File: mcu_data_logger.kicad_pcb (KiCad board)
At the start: 2 copper layers, 29 parts, among them J1 Conn_01x04_Pin, J2 Conn_01x09_Pin, J3 Conn_01x04_Pin, J4 Conn_02x03_Odd_Even, U1 24LC1025, U2 DS1337S_, U3 24LC1025, U4 ATMEGA328P-AU, Y1 32.768 kHz, Y2 16MHz

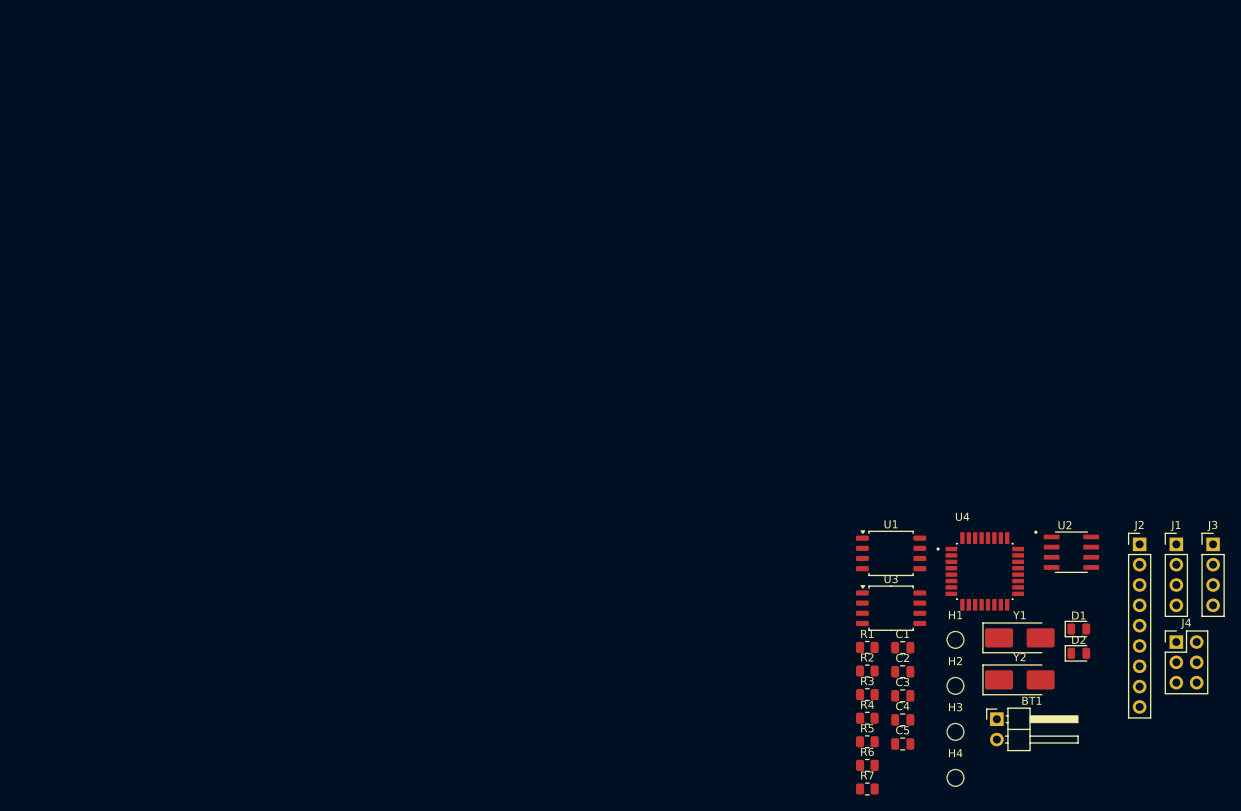
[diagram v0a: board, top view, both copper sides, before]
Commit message: Partial arrangement of footprints and change of battery component footprint
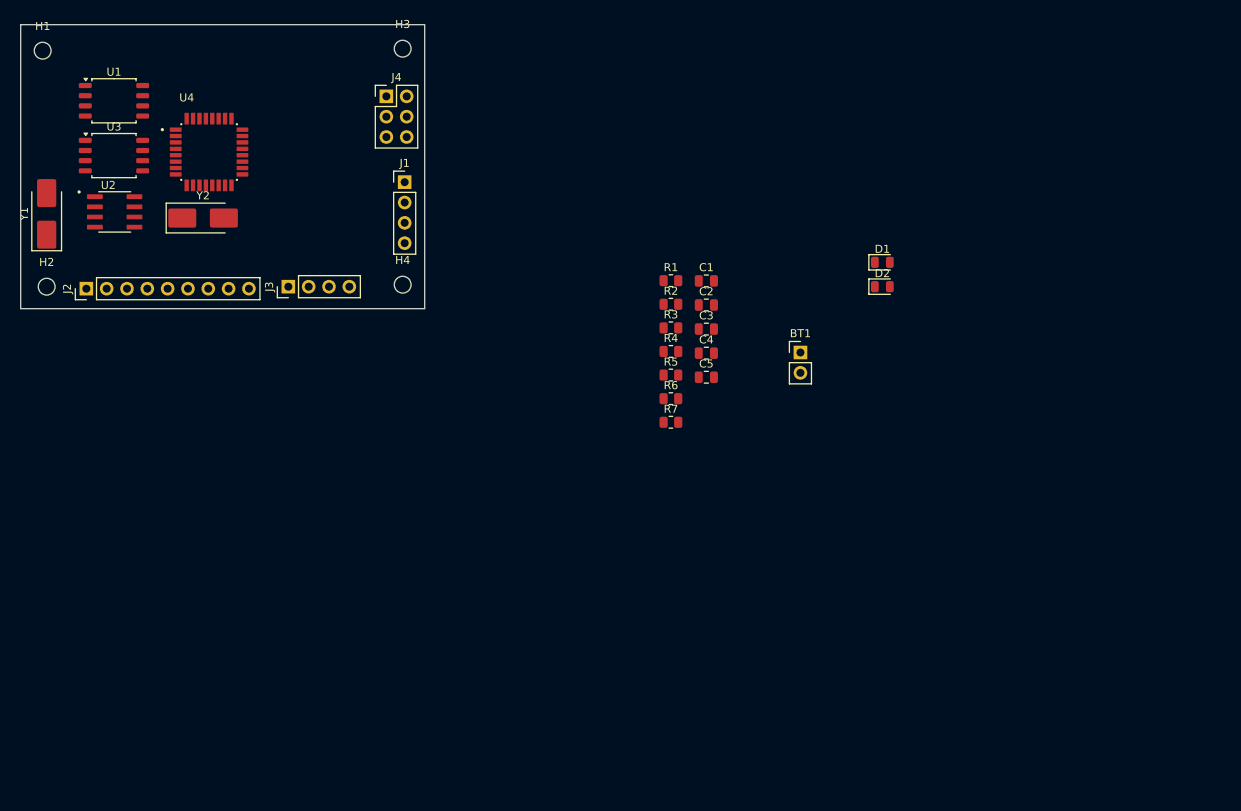
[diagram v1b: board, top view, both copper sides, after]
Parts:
- BT1: footprint Connector_PinHeader_2.54mm:PinHeader_1x02_P2.54mm_Horizontal -> Connector_PinHeader_2.54mm:PinHeader_1x02_P2.54mm_Vertical
- moved H1 135.8 mm to (73.2, 59.8)
- moved J2 135.5 mm to (78.7, 89.5), turned to 90 degrees
- moved Y1 132.7 mm to (73.8, 80.2), turned to 90 degrees
- moved U2 126.9 mm to (82.2, 79.9)
- moved H2 124.1 mm to (73.8, 89.2)
- moved J4 120.0 mm to (116.2, 65.5)
- moved J3 120.0 mm to (104.0, 89.2), turned to 90 degrees
- moved Y2 117.3 mm to (93.3, 80.7)
- moved U1 112.4 mm to (82.2, 66.0)
- moved U3 112.4 mm to (82.2, 72.9)
- moved U4 110.2 mm to (94.0, 72.4)
- moved H3 109.9 mm to (118.2, 59.5)
- moved J1 106.6 mm to (118.5, 76.2)
- moved H4 92.6 mm to (118.2, 89.0)
- moved R1 52.0 mm to (151.8, 88.5)
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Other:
- board outline added: 50.5 x 35.5 mm

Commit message: footprint arrangement and placement complete
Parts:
- moved BT1 97.5 mm to (75.2, 67.2)
- moved D2 76.6 mm to (105.5, 62.0), turned to 180 degrees
- moved D1 73.9 mm to (109.5, 62.0)
- moved R1 71.1 mm to (81.0, 82.0)
- moved C1 70.0 mm to (91.5, 61.8)
- moved C3 68.8 mm to (95.7, 61.8)
- moved C5 68.3 mm to (100.0, 61.8)
- moved R2 67.2 mm to (85.2, 82.0), turned to 180 degrees
- moved R7 61.0 mm to (105.5, 66.5)
- moved R5 54.1 mm to (109.5, 66.5)
- moved R4 53.4 mm to (105.5, 70.8), turned to 180 degrees
- moved C4 53.3 mm to (105.5, 81.0), turned to 180 degrees
- moved R6 53.1 mm to (109.8, 70.8)
- moved C2 52.6 mm to (105.5, 77.5)
- moved R3 50.5 mm to (105.5, 74.2)
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- renumbered D2 to D1, D1 to D2
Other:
- board size 50.5 x 35.5 mm -> 48 x 34.5 mm

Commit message: initial routing done
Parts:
- moved U1 6.87 mm to (82.7, 69.6)
- moved U3 6.85 mm to (83.2, 62.8)
- moved H4 1.82 mm to (117.0, 90.0)
- moved H2 1.75 mm to (73.7, 90.0)
- moved H3 0.48 mm to (117.0, 59.8)
- moved H1 0.23 mm to (73.7, 59.8)
- moved J2 0.22 mm to (78.5, 88.5)
- moved J3 0.22 mm to (103.7, 88.2)
- moved C1 0.18 mm to (91.5, 62.0)
- moved C3 0.18 mm to (95.8, 62.0)
- moved C5 0.18 mm to (100.0, 62.0)
- turned C2 to 180 degrees
- turned D2 to 0 degrees
- turned R3 to 180 degrees
- turned R5 to 180 degrees
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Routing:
- net /Vcc: track 0.00 -> 114.3 mm, vias 0 -> 1
- net /SCK: track 0.00 -> 95.5 mm, vias 0 -> 3
- net Net-(BT1-+): track 0.00 -> 56.7 mm, vias 0 -> 3
- net /SDA: track 0.00 -> 55.7 mm, vias 0 -> 2
- net GND: track 0.00 -> 50.4 mm, vias 0 -> 6
- net /TX: track 0.00 -> 30.0 mm, vias 0 -> 1
- net /RX: track 0.00 -> 28.7 mm, vias 0 -> 1
- net /D2: track 0.00 -> 26.6 mm, vias 0 -> 1
- net /MOSI: track 0.00 -> 26.1 mm
- net /RESET: track 0.00 -> 26.0 mm, vias 0 -> 2
- net Net-(U4-PB7): track 0.00 -> 25.6 mm, vias 0 -> 2
- net /D3: track 0.00 -> 25.2 mm
- net Net-(U4-PB6): track 0.00 -> 23.8 mm
- net /D4: track 0.00 -> 22.2 mm
- net /MISO: track 0.00 -> 21.2 mm, vias 0 -> 1
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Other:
- board size 48 x 34.5 mm -> 48 x 36 mm

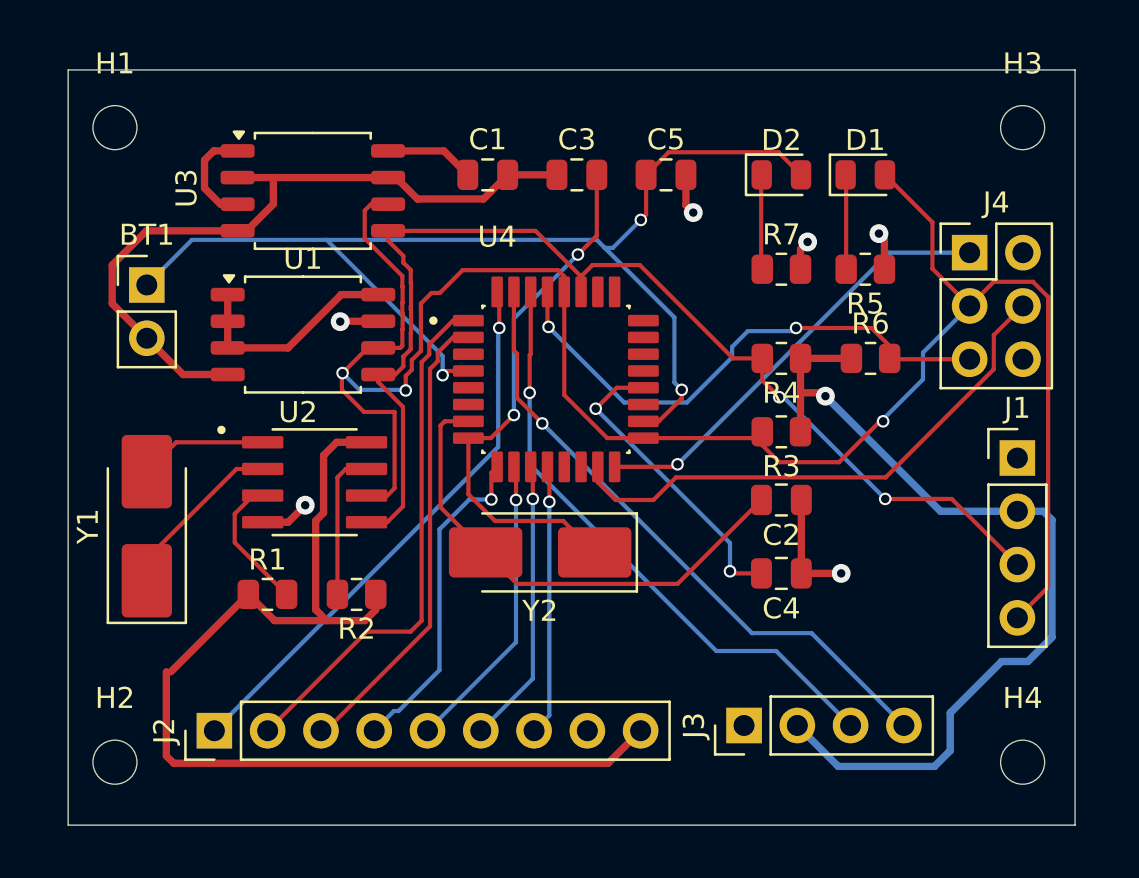
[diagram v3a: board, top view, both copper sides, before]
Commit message: added copper fills for the /Vcc and GND nets, front and back copper layer respectively
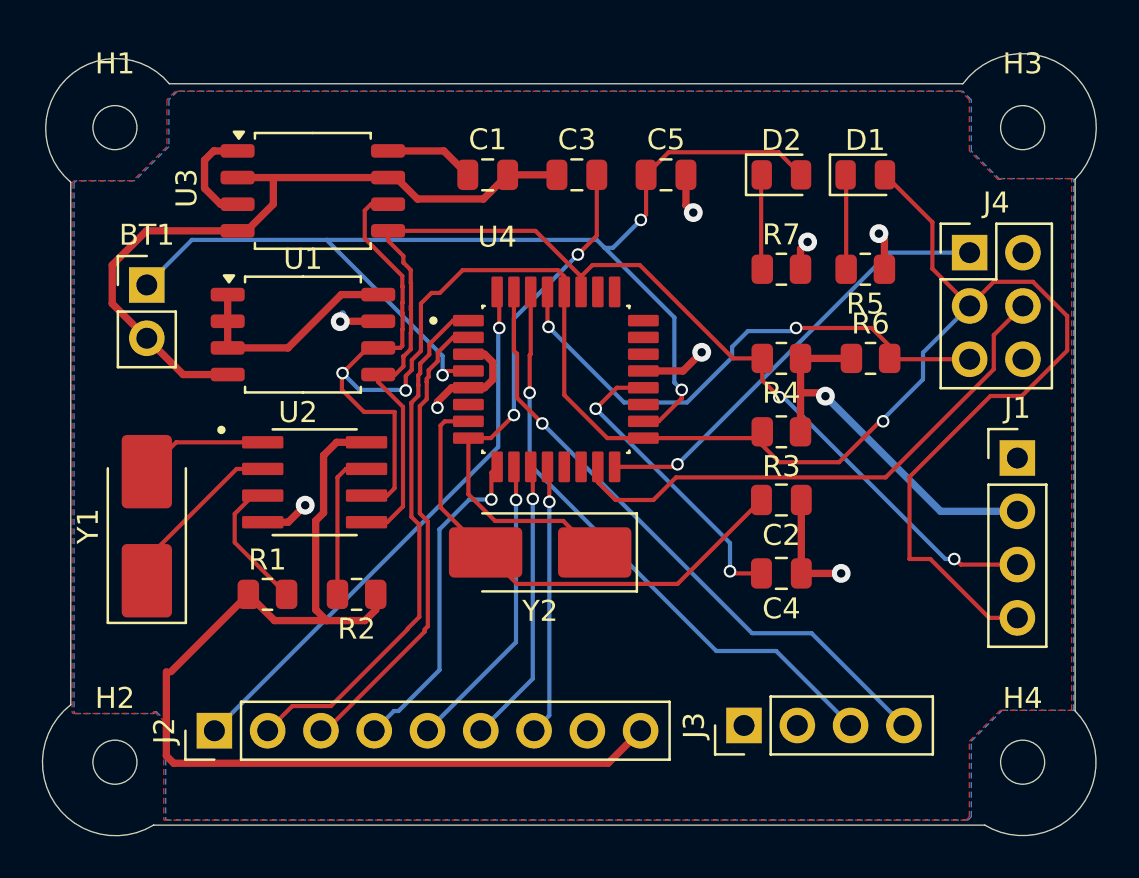
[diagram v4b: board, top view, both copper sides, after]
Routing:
- net /Vcc: track 114.3 -> 90.3 mm
- net GND: track 50.4 -> 59.6 mm, vias 6 -> 8
- net /SCK: track 95.5 -> 102.8 mm
- added copper zone on F.Cu, net /Vcc
- added copper zone on B.Cu, net GND
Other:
- board size 48 x 36 mm -> 50.2 x 37.3 mm

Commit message: assigned the Vcc net to the BT1 positive terminal in the Schematic Editor which resulted in a lot of bug fixing and rerouting in the PCB Editor
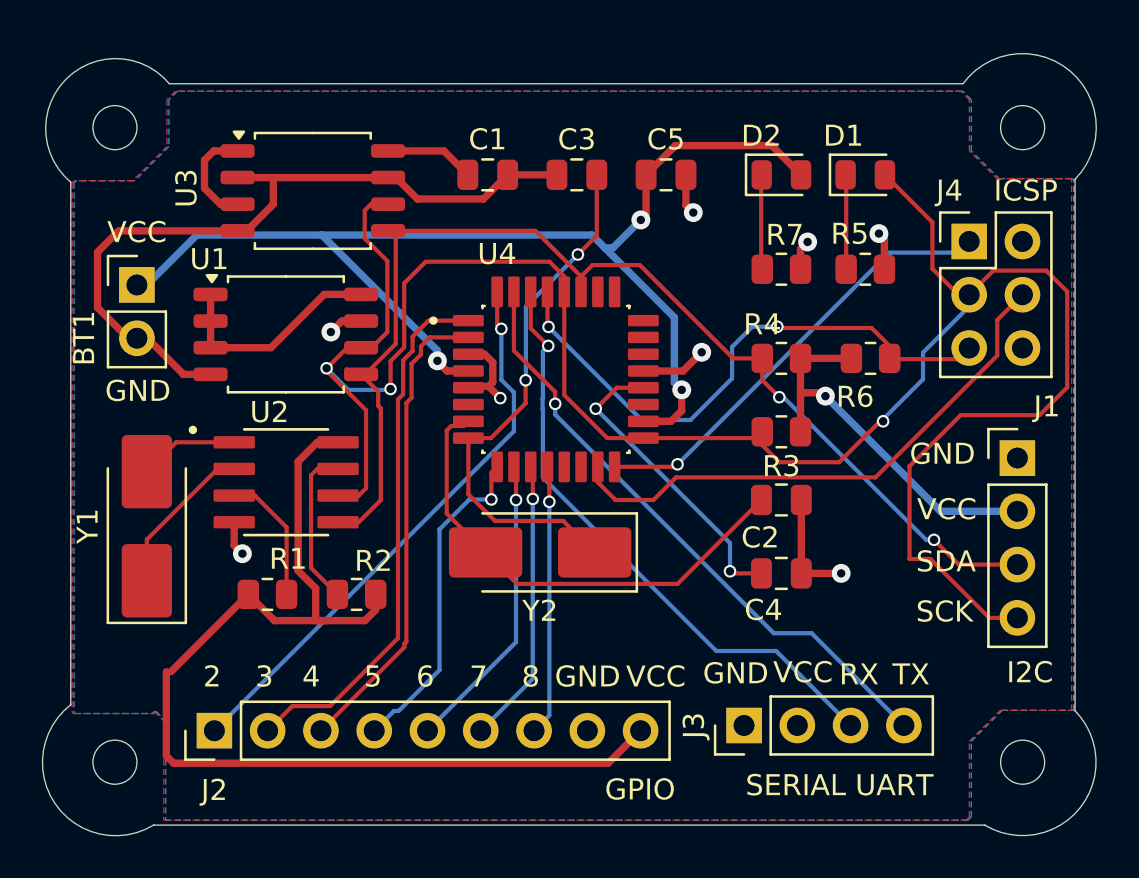
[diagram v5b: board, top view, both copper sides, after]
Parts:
- moved U2 1.36 mm to (81.9, 76.7)
- moved U1 0.82 mm to (81.9, 69.6)
- moved J4 0.53 mm to (114.5, 65.2)
- moved BT1 0.47 mm to (74.8, 67.2)
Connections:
- BT1 pad 1: Net-(BT1-+) -> /Vcc
- C5 pad 1: Net-(BT1-+) -> /Vcc
- D2 pad 2: Net-(BT1-+) -> /Vcc
- U4 pad 18: Net-(BT1-+) -> /Vcc
- U4 pad 4: Net-(BT1-+) -> /Vcc
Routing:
- net /Vcc: track 90.3 -> 148.4 mm, vias 1 -> 4
- net Net-(BT1-+): track 56.7 -> 0.00 mm, vias 3 -> 0
- net /SCK: track 102.8 -> 105.8 mm
- net GND: track 59.6 -> 57.5 mm
- net /RESET: track 26.0 -> 27.5 mm
- net Net-(U2-X1): track 6.10 -> 4.74 mm
- net Net-(U2-SQW/~INT): track 7.13 -> 7.99 mm
- net Net-(U2-X2): track 8.35 -> 7.52 mm
- net /D2: track 26.6 -> 27.3 mm
- net /TX: track 30.0 -> 29.4 mm
- net Net-(U4-PB6): track 23.8 -> 23.2 mm
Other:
- board text added: "2"
- board text added: "3"
- board text added: "4"
- board text added: "5"
- board text added: "6"
- board text added: "7"
- board text added: "8"
- board text added: "GND"
- board text added: "GPIO"
- board text added: "I2C"
- board text added: "ICSP"
- board text added: "MISO"
- board text added: "MOSI"
- board text added: "RESET"
- board text added: "RX"
- board text added: "SCK"
- board text added: "SDA"
- board text added: "SERIAL UART"
- board text added: "TX"
- board text added: "VCC"

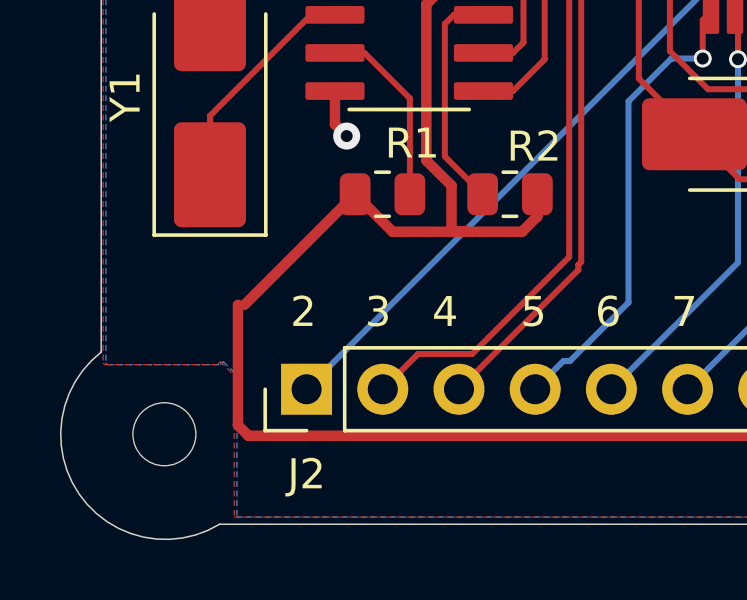
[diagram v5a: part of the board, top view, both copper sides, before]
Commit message: added KiCad logo silkscreen
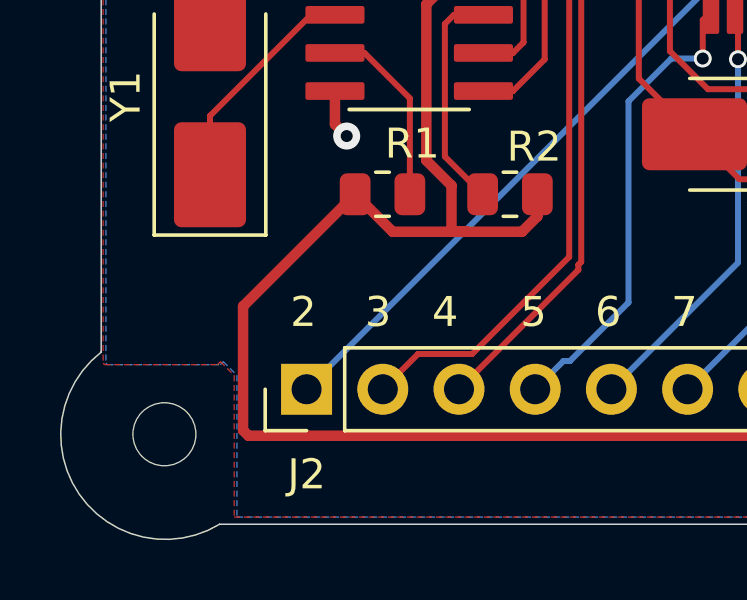
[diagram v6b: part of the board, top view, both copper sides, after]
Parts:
- added REF**: KiCad-Logo2_5mm_SilkScreen, Symbol:KiCad-Logo2_5mm_SilkScreen, B.Cu at (93.2, 73.5)

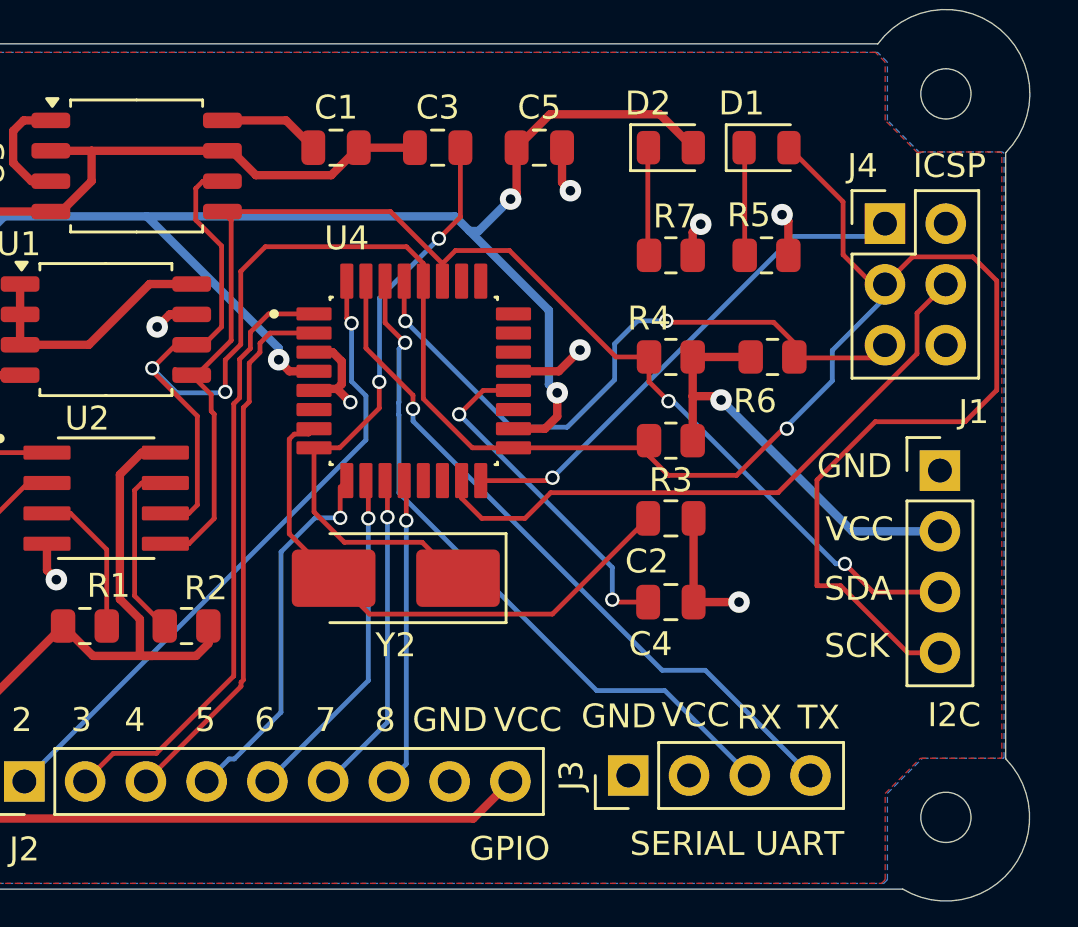
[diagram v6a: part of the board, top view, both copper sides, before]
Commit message: fixed pcb design (routing) after fixing the net labels in the schematic editor
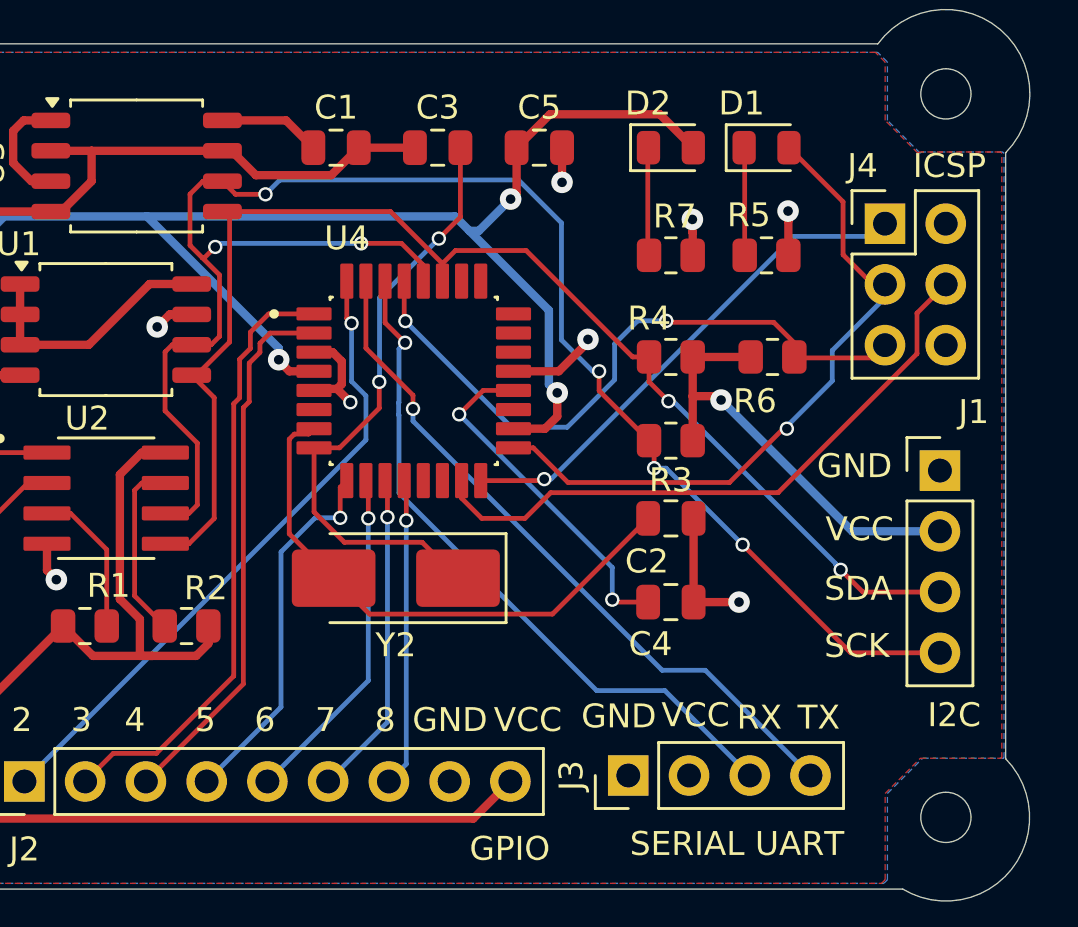
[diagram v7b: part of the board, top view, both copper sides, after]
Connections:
- J1 pad 4: /SCK -> /SCL
- R3 pad 2: /SCK -> /SCL
- U1 pad 6: /SCK -> /SCL
- U2 pad 6: /SCK -> /SCL
- U3 pad 6: /SCK -> /SCL
- U4 pad 28: /SCK -> /SCL
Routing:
- net /SCK: track 105.8 -> 28.9 mm, vias 3 -> 1
- net /SCL: track 0.00 -> 72.1 mm, vias 0 -> 6
